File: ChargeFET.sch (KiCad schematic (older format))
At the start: 7 parts, among them Q1 DMP6023LE-13, Q2 DMN55D0UT-7

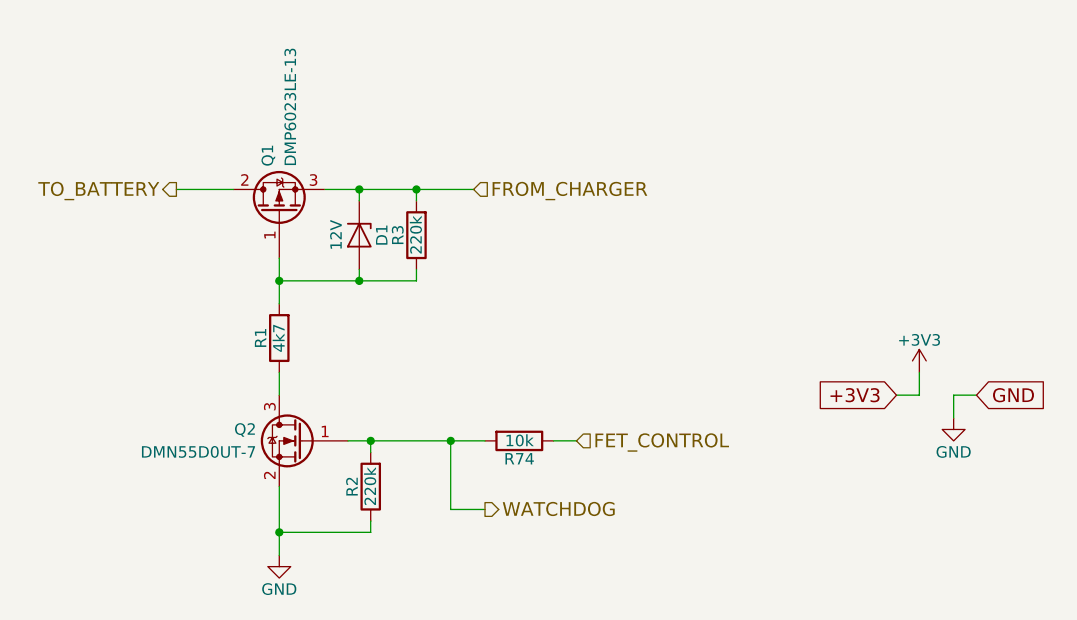
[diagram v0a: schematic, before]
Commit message: HW 0.2 finalized schematic and pcb files, BOM needs to be checked
Lots of major and little problems fixed found in the 0.1

Major changes:
-LTC6803-3 footprint changed to it's correct one
-Boost converter layout and capacitor optimization
-MCU switched from STM32F070CBT6 to ultra low power STM32L433CCT6 to improve sleep state power consumption
-Button/LED + Comms connectors switched from THT JST-XH to SMD JST-PH
-CAN-bus support added
-Changed power regulator setup for "always on"

Minor changes:
-Changed cell balance resistor sizes from 0603 to 0402 in order to get a bit more breathing room during soldering
-External oscillator removed from MCU, because new one has everything available internally
-Comms connector has USART or CAN available via solder bridges
-Sense resistors switched to higher resistance ones to lower deep sleep standby current
-etc.
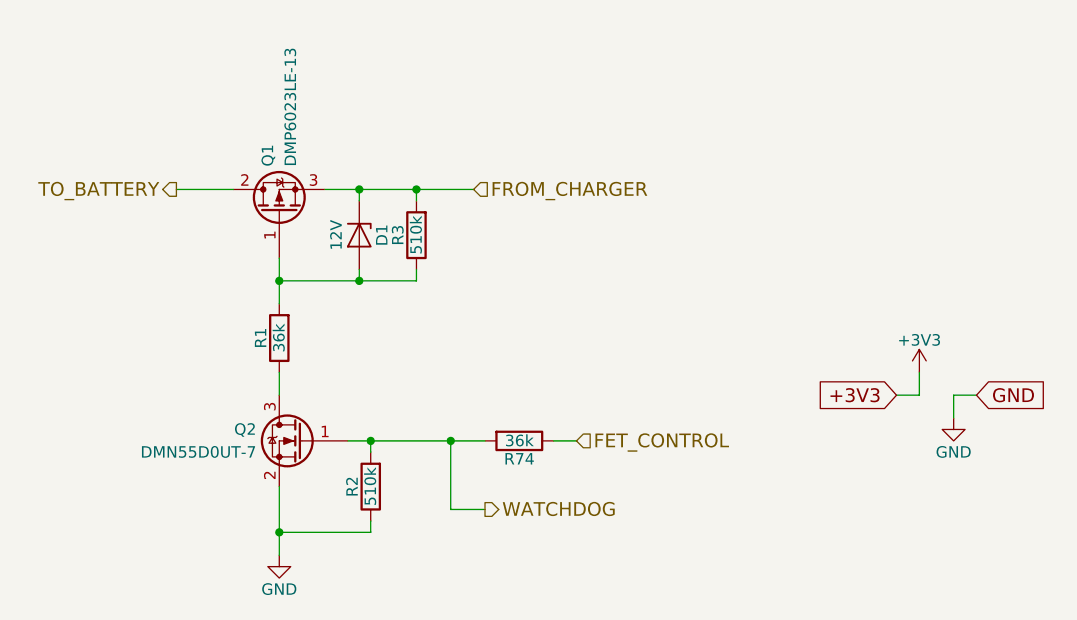
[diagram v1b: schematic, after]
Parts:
- R1: value 4k7 -> 36k; MFG RC0603FR-074K7L -> ANY; Tol. (none) -> 1%
- R2, R3: value 220k -> 510k; MFG RC0603FR-07220KL -> ANY; Tol. (none) -> 1%
- R74: value 10k -> 36k; MFG RC0603FR-0710KL -> ANY; Tol. (none) -> 1%
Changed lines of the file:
@@
 LIBS:valves
 LIBS:Custom_comp_lib
-LIBS:FlexiBMS_01-cache
+LIBS:FlexiBMS-cache
 EELAYER 25 0
 EELAYER END
@@
 Title "FlexiBMS"
 Date "2018-02-22"
-Rev "0.1"
+Rev "0.2"
 Comp ""
 Comment1 ""
@@
 P 5350 3350
 F 0 "R3" V 5430 3350 50  0000 C CNN
-F 1 "220k" V 5350 3350 50  0000 C CNN
+F 1 "510k" V 5350 3350 50  0000 C CNN
 F 2 "Resistors_SMD:R_0603" V 5280 3350 50  0001 C CNN
 F 3 "" H 5350 3350 50  0001 C CNN
-F 4 "RC0603FR-07220KL" V 5350 3350 60  0001 C CNN "MFG"
+F 4 "ANY" V 5350 3350 60  0001 C CNN "MFG"
+F 5 "1%" V 5350 3350 60  0001 C CNN "Tol."
 	1    5350 3350
 	-1   0    0    1
@@
 P 4750 3800
 F 0 "R1" V 4830 3800 50  0000 C CNN
-F 1 "4k7" V 4750 3800 50  0000 C CNN
+F 1 "36k" V 4750 3800 50  0000 C CNN
 F 2 "Resistors_SMD:R_0603" V 4680 3800 50  0001 C CNN
 F 3 "" H 4750 3800 50  0001 C CNN
-F 4 "RC0603FR-074K7L" V 4750 3800 60  0001 C CNN "MFG"
+F 4 "ANY" V 4750 3800 60  0001 C CNN "MFG"
+F 5 "1%" V 4750 3800 60  0001 C CNN "Tol."
 	1    4750 3800
 	-1   0    0    1
@@
 P 5150 4450
 F 0 "R2" V 5230 4450 50  0000 C CNN
-F 1 "220k" V 5150 4450 50  0000 C CNN
+F 1 "510k" V 5150 4450 50  0000 C CNN
 F 2 "Resistors_SMD:R_0603" V 5080 4450 50  0001 C CNN
 F 3 "" H 5150 4450 50  0001 C CNN
-F 4 "RC0603FR-07220KL" V 5150 4450 60  0001 C CNN "MFG"
+F 4 "ANY" V 5150 4450 60  0001 C CNN "MFG"
+F 5 "1%" V 5150 4450 60  0001 C CNN "Tol."
 	1    5150 4450
 	-1   0    0    1
 $EndComp
 $Comp
-L GND #PWR067
+L GND #PWR070
 U 1 1 5A859271
 P 4750 4750
-F 0 "#PWR067" H 4750 4500 50  0001 C CNN
+F 0 "#PWR070" H 4750 4500 50  0001 C CNN
 F 1 "GND" H 4750 4600 50  0000 C CNN
 F 2 "" H 4750 4750 50  0001 C CNN
@@
 GND
 $Comp
-L GND #PWR068
+L GND #PWR071
 U 1 1 5A85A141
 P 7700 4150
-F 0 "#PWR068" H 7700 3900 50  0001 C CNN
+F 0 "#PWR071" H 7700 3900 50  0001 C CNN
 F 1 "GND" H 7700 4000 50  0000 C CNN
 F 2 "" H 7700 4150 50  0001 C CNN
@@
 $EndComp
 $Comp
-L +3V3 #PWR069
+L +3V3 #PWR072
 U 1 1 5A85A167
 P 7550 3950
-F 0 "#PWR069" H 7550 3800 50  0001 C CNN
+F 0 "#PWR072" H 7550 3800 50  0001 C CNN
 F 1 "+3V3" H 7550 4090 50  0000 C CNN
 F 2 "" H 7550 3950 50  0001 C CNN
@@
 P 5800 4250
 F 0 "R74" V 5880 4250 50  0000 C CNN
-F 1 "10k" V 5800 4250 50  0000 C CNN
+F 1 "36k" V 5800 4250 50  0000 C CNN
 F 2 "Resistors_SMD:R_0603" V 5730 4250 50  0001 C CNN
 F 3 "" H 5800 4250 50  0001 C CNN
-F 4 "RC0603FR-0710KL" V 5800 4250 60  0001 C CNN "MFG"
+F 4 "ANY" V 5800 4250 60  0001 C CNN "MFG"
+F 5 "1%" V 5800 4250 60  0001 C CNN "Tol."
 	1    5800 4250
 	0    1    1    0
